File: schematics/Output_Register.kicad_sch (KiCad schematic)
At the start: 34 parts, among them SW1 SW_SPDT, U1 74LS273, U10 74LS08, U2 28C64, U3 D168K, U4 D168K, U5 D168K, U6 D168K, U7 74LS139, U8 74LS107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

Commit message: feat: updated electrical diagrams & individual part list
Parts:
- added C5, C6: 0.1uF, symbol Device:C
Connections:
- net +5V: now also C5.2, C6.2
- net GND: now also C5.1, C6.1

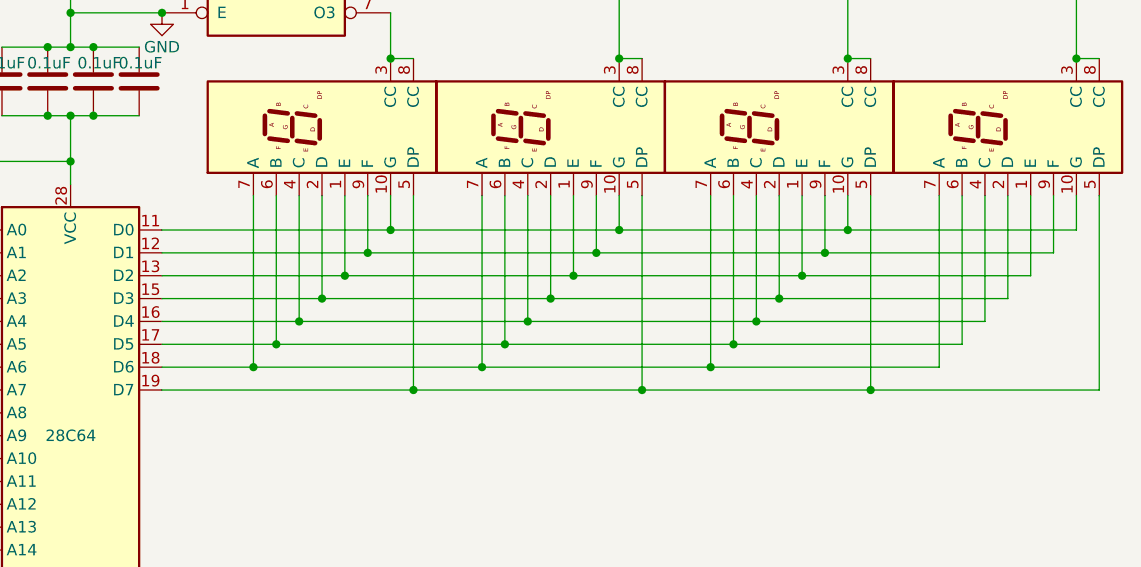
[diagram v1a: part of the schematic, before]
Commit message: Updated schematics and README
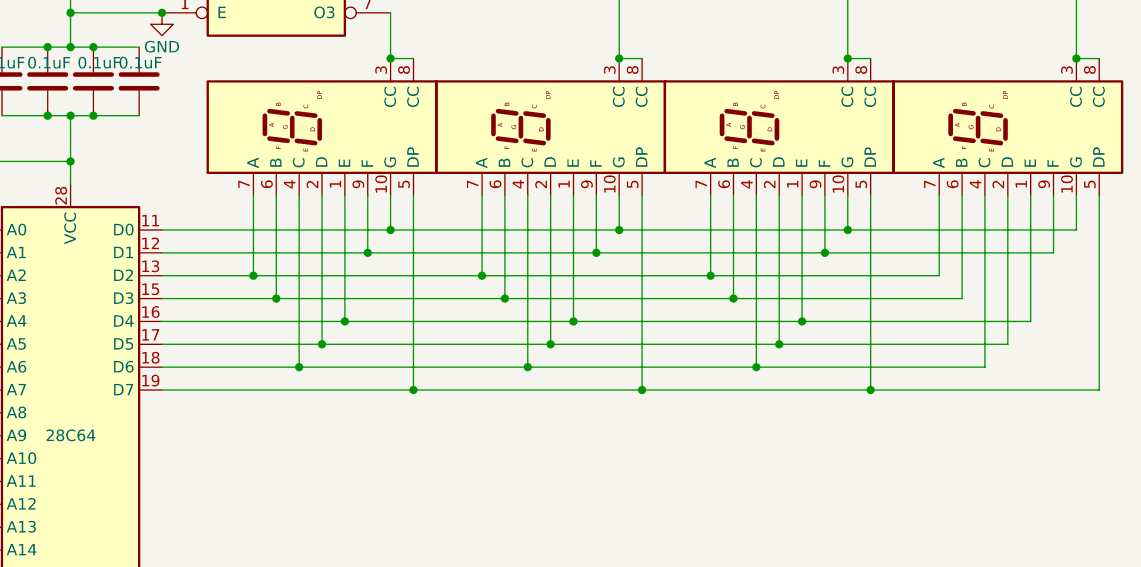
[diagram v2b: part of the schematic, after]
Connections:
- net at U3.1 (E), U4.1 (E), U5.1 (E)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: now also U2.16 (D4); no longer U2.13 (D2)
- net at U3.2 (D), U4.2 (D), U5.2 (D)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: now also U2.17 (D5); no longer U2.15 (D3)
- net at U3.4 (C), U4.4 (C), U5.4 (C)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: now also U2.18 (D6); no longer U2.16 (D4)
- net at U3.6 (B), U4.6 (B), U5.6 (B)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: now also U2.15 (D3); no longer U2.17 (D5)
- net at U3.7 (A), U4.7 (A), U5.7 (A)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: now also U2.13 (D2); no longer U2.18 (D6)
